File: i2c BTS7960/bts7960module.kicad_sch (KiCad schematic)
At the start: 43 parts, among them J10 Conn_01x02, J2 Conn_01x04, J5 jst, U10 BTS7960B, U11 BTS7960B, U7 74AHC244, U8 BTS7960B, U9 BTS7960B

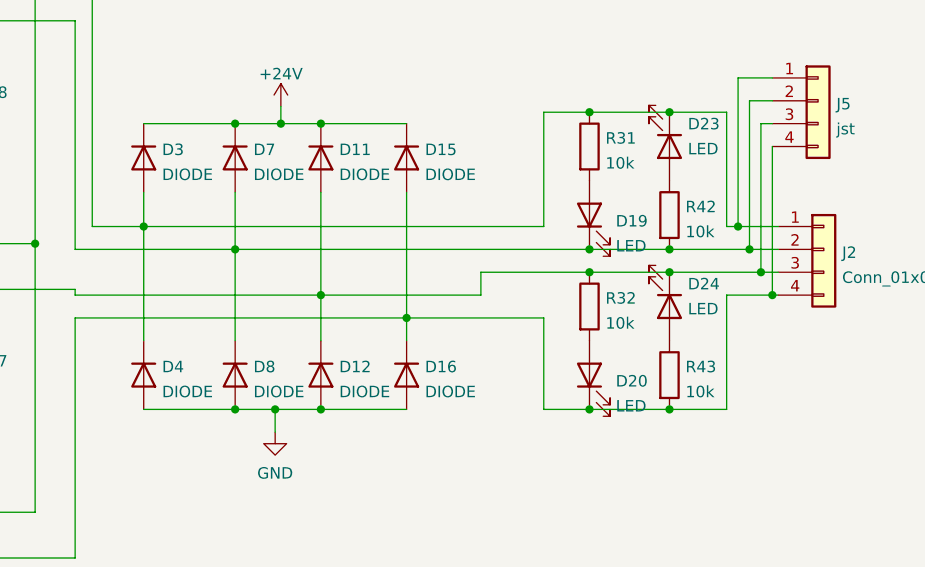
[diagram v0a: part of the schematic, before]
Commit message: motor controller DFM
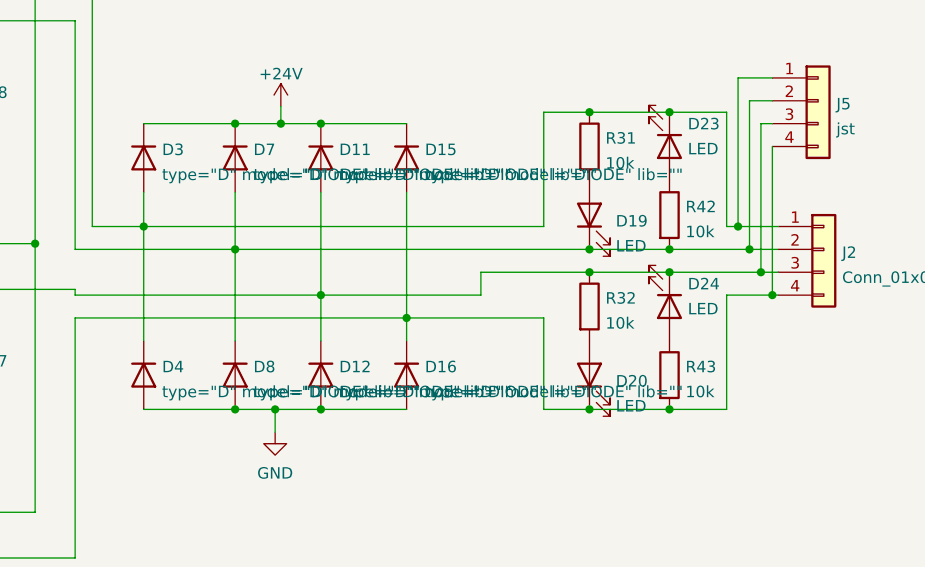
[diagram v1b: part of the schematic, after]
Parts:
- D11, D12, D15, D16, D3, D4, D7, D8: value DIODE -> ${SIM.PARAMS}; Spice_Netlist_Enabled Y -> (none); Spice_Primitive D -> (none)
